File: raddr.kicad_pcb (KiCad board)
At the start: 2 copper layers, 25.4 x 25.4 mm, 7 parts, among them U1 PY32F002AL1xS

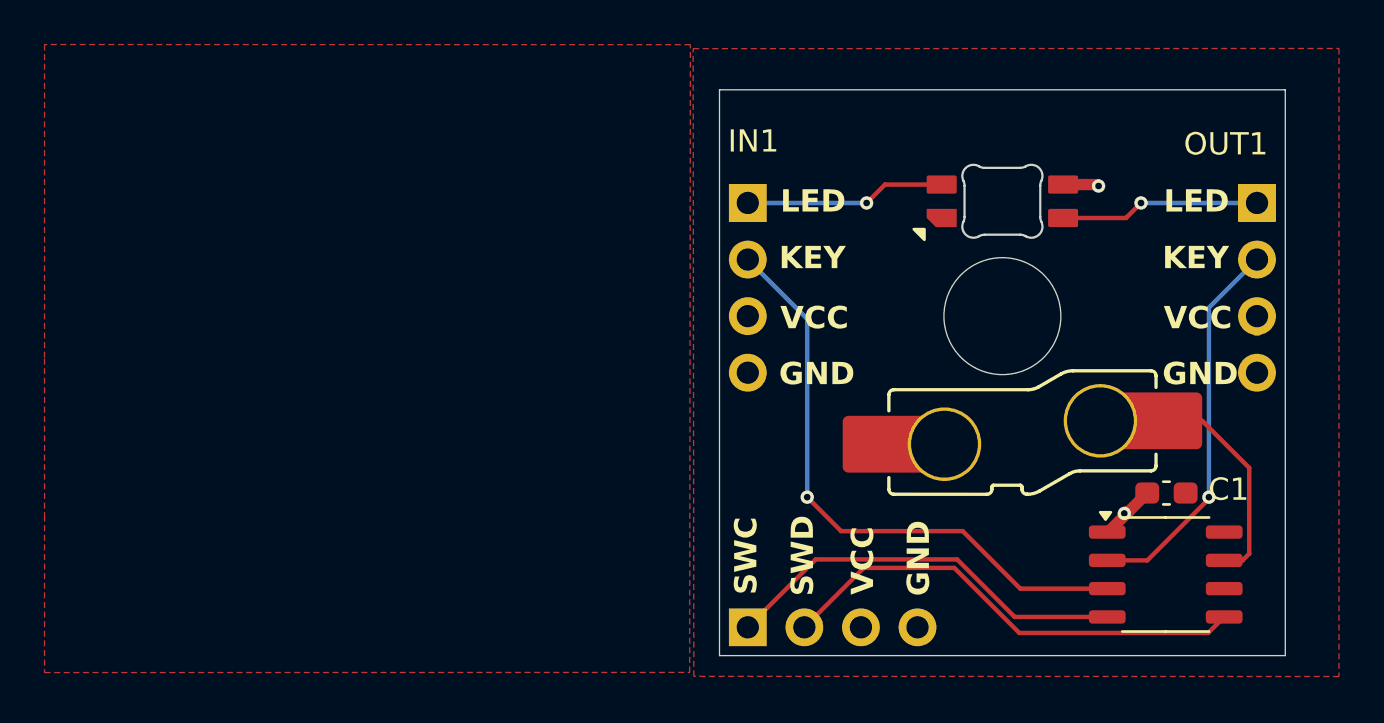
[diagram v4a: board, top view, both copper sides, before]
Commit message: fix power plane
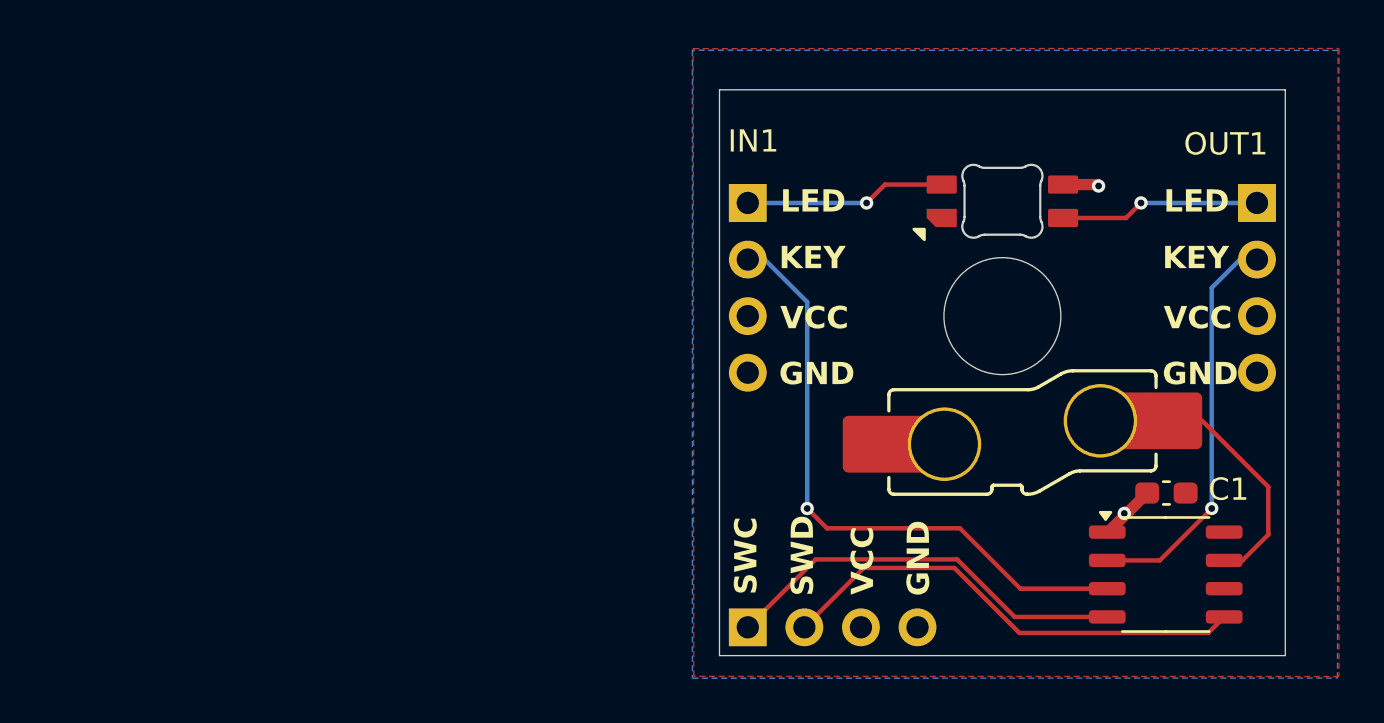
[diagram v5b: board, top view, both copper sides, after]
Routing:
- net KEY_DOUT: track 17.5 -> 18.3 mm
- net KEY_DIN: track 27.4 -> 28.2 mm
- net SWITCH: track 9.41 -> 10.1 mm
- net +5VD: track 4.93 -> 4.28 mm
- added copper zone on B.Cu, net +5VD
- removed copper zone on F.Cu, net +5VD
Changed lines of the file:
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@@
 		(tags "kailh choc 6028 rearmount rear mount led rgb backlight")
 		(property "Reference" "LED1"
-			(at 0 -2.6 360)
+			(at 0 -2.6 0)
 			(layer "F.SilkS")
 			(hide yes)
@@
 		)
 		(property "Value" "choc_SK6812MINI-E"
-			(at 0 18 360)
+			(at 0 18 0)
 			(layer "F.Fab")
 			(hide yes)
@@
 		(fp_arc
 			(start 1.699999 -0.702841)
-			(mid 1.71253 -0.814066)
+			(mid 1.712533 -0.814065)
 			(end 1.749484 -0.919719)
 			(stroke
@@
 		(tags "SOP SO")
 		(property "Reference" "U1"
-			(at 0 -3.4 360)
+			(at 0 -3.4 0)
 			(layer "F.SilkS")
 			(hide yes)
@@
 		)
 		(property "Value" "PY32F002AL1xS"
-			(at 0 3.4 360)
+			(at 0 3.4 0)
 			(layer "F.Fab")
 			(hide yes)
@@
 		)
 		(fp_text user "${REFERENCE}"
-			(at 0 0 360)
+			(at 0 0 0)
 			(layer "F.Fab")
 			(effects
@@
 		(fp_arc
 			(start 0.803483 7.591366)
-			(mid 0.856539 7.613325)
+			(mid 0.856533 7.613316)
 			(end 0.878483 7.666366)
 			(stroke
@@
 		(fp_arc
 			(start 2.63142 2.597493)
-			(mid 2.890651 2.490108)
+			(mid 2.890649 2.490103)
 			(end 3.168841 2.453491)
 			(stroke
@@
 		(fp_arc
 			(start 3.023183 7.070426)
-			(mid 3.246257 6.978023)
+			(mid 3.246259 6.978033)
 			(end 3.485647 6.946509)
 			(stroke
@@
 		(fp_arc
 			(start 0.803483 7.591366)
-			(mid 0.856539 7.613325)
+			(mid 0.856533 7.613316)
 			(end 0.878483 7.666366)
 			(stroke
@@
 		(fp_arc
 			(start 2.63142 2.597493)
-			(mid 2.890651 2.490108)
+			(mid 2.890649 2.490103)
 			(end 3.168841 2.453491)
 			(stroke
@@
 		(fp_arc
 			(start 3.023183 7.070426)
-			(mid 3.246257 6.978023)
+			(mid 3.246259 6.978033)
 			(end 3.485647 6.946509)
 			(stroke
@@
 		(fp_arc
 			(start 0.803483 7.591366)
-			(mid 0.856539 7.613325)
+			(mid 0.856533 7.613316)
 			(end 0.878483 7.666366)
 			(stroke
@@
 		(fp_arc
 			(start 2.63142 2.597493)
-			(mid 2.890651 2.490108)
+			(mid 2.890649 2.490103)
 			(end 3.168841 2.453491)
 			(stroke
@@
 		(fp_arc
 			(start 3.023183 7.070426)
-			(mid 3.246257 6.978023)
+			(mid 3.246259 6.978033)
 			(end 3.485647 6.946509)
 			(stroke
@@
 		)
 		(property "Value" "C_Polarized"
-			(at 0 1.43 360)
+			(at 0 1.43 0)
 			(layer "F.Fab")
 			(hide yes)
@@
 		)
 		(fp_text user "${REFERENCE}"
-			(at 0 0 360)
+			(at 0 0 0)
 			(layer "F.Fab")
 			(effects
@@
 	)
 	(segment
-		(start 20.32 5.08)
-		(end 20.32 5.725506)
-		(width 0.508)
-		(layer "B.Cu")
-		(net 2)
-	)
-	(segment
 		(start 19.6462 0.6738)
 		(end 20.32 0)
@@
 	(segment
 		(start 13.5968 16.0448)
-		(end 15.396522 16.0448)
-		(width 0.2)
-		(layer "F.Cu")
-		(net 4)
-	)
-	(segment
-		(start 18.161 13.280322)
-		(end 18.161 13.208)
+		(end 15.9592 16.0448)
 		(width 0.2)
 		(layer "F.Cu")
@@
 	)
 	(segment
-		(start 15.396522 16.0448)
-		(end 18.161 13.280322)
+		(start 15.9592 16.0448)
+		(end 18.288 13.716)
 		(width 0.2)
 		(layer "F.Cu")
@@
 	)
 	(via
-		(at 18.161 13.208)
+		(at 18.288 13.716)
 		(size 0.6)
 		(drill 0.3)
@@
 	)
 	(segment
-		(start 18.161 4.699)
-		(end 18.161 13.208)
+		(start 18.288 3.81)
+		(end 18.288 13.716)
 		(width 0.2)
 		(layer "B.Cu")
@@
 	(segment
 		(start 20.32 2.54)
-		(end 18.161 4.699)
+		(end 19.558 2.54)
+		(width 0.2)
+		(layer "B.Cu")
+		(net 4)
+	)
+	(segment
+		(start 19.558 2.54)
+		(end 18.288 3.81)
 		(width 0.2)
 		(layer "B.Cu")
@@
 	(segment
 		(start 9.6948 17.3148)
-		(end 7.112 14.732)
-		(width 0.2)
-		(layer "F.Cu")
-		(net 6)
-	)
-	(segment
-		(start 13.5968 17.3148)
-		(end 9.6948 17.3148)
+		(end 6.985 14.605)
 		(width 0.2)
 		(layer "F.Cu")
@@
 	)
 	(segment
-		(start 1.651 14.732)
-		(end 0.127 13.208)
+		(start 6.985 14.605)
+		(end 1.016004 14.605)
 		(width 0.2)
 		(layer "F.Cu")
@@
 	)
 	(segment
-		(start 7.112 14.732)
-		(end 1.651 14.732)
+		(start 13.5968 17.3148)
+		(end 9.6948 17.3148)
 		(width 0.2)
 		(layer "F.Cu")
@@
 		(net 6)
 	)
+	(segment
+		(start 1.016004 14.605)
+		(end 0.127 13.715996)
+		(width 0.2)
+		(layer "F.Cu")
+		(net 6)
+	)
 	(via
-		(at 0.127 13.208)
+		(at 0.127 13.715996)
 		(size 0.6)
 		(drill 0.3)
@@
 	)
 	(segment
-		(start 0.127 5.207)
-		(end 0.127 13.208)
+		(start -2.54 2.54)
+		(end -1.778 2.54)
 		(width 0.2)
 		(layer "B.Cu")
@@
 	)
 	(segment
-		(start -2.54 2.54)
-		(end 0.127 5.207)
+		(start 0.127 4.445)
+		(end 0.127 13.715996)
 		(width 0.2)
 		(layer "B.Cu")
@@
 	)
 	(segment
-		(start 19.9718 11.891801)
-		(end 19.9718 15.744799)
+		(start -1.778 2.54)
+		(end 0.127 4.445)
+		(width 0.2)
+		(layer "B.Cu")
+		(net 6)
+	)
+	(segment
+		(start 16.535 9.78)
+		(end 17.859999 9.78)
 		(width 0.2)
 		(layer "F.Cu")
@@
 	(segment
 		(start 17.859999 9.78)
-		(end 19.9718 11.891801)
+		(end 20.828 12.748001)
 		(width 0.2)
 		(layer "F.Cu")
@@
 	)
 	(segment
-		(start 19.9718 15.744799)
+		(start 20.828 14.888599)
 		(end 19.671799 16.0448)
 		(width 0.2)
@@
 	)
 	(segment
-		(start 16.535 9.78)
-		(end 17.859999 9.78)
+		(start 20.828 12.748001)
+		(end 20.828 14.888599)
 		(width 0.2)
 		(layer "F.Cu")
@@
 	)
 	(zone
-		(net 2)
-		(net_name "+5VD")
+		(net 1)
+		(net_name "GND")
 		(layer "F.Cu")
-		(name "POWER plane")
+		(name "Ground plane")
 		(hatch edge 0.5)
 		(connect_pads
@@
 		(polygon
 			(pts
-				(xy -5.117238 -7.105483) (xy -34.110476 -7.112) (xy -34.110476 6.985) (xy -34.110476 14.0335) (xy -34.110476 21.082)
-				(xy -5.148316 21.075184)
+				(xy -4.993238 -6.928883) (xy 24 -6.9354) (xy 24 21.2586) (xy -4.96216 21.251784)
 			)
 		)
 	)
 	(zone
-		(net 1)
-		(net_name "GND")
-		(layer "F.Cu")
-		(name "Ground plane")
+		(net 2)
+		(net_name "+5VD")
+		(layer "B.Cu")
+		(name "POWER plane")
 		(hatch edge 0.5)
 		(connect_pads
@@
 		(polygon
 			(pts
-				(xy -4.993238 -6.928883) (xy 24 -6.9354) (xy 24 21.2586) (xy -4.96216 21.251784)
+				(xy 23.965762 -6.851483) (xy -5.027476 -6.858) (xy -5.027476 7.239) (xy -5.027476 14.2875) (xy -5.027476 21.336)
+				(xy 23.934684 21.329184)
 			)
 		)

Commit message: silk screen and stuff
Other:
- board text added: "RABIES rev 1/N WFP-YBS 20241030 {dblquote}Waarschijnlijk ruk{dblquote}"
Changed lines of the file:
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@@
 			(plot_on_all_layers_selection 0x0000000_00000000)
 			(disableapertmacros no)
-			(usegerberextensions no)
-			(usegerberattributes yes)
-			(usegerberadvancedattributes yes)
-			(creategerberjobfile yes)
+			(usegerberextensions yes)
+			(usegerberattributes no)
+			(usegerberadvancedattributes no)
+			(creategerberjobfile no)
 			(dashed_line_dash_ratio 12.000000)
 			(dashed_line_gap_ratio 3.000000)
@@
 			(psa4output no)
 			(plotreference yes)
-			(plotvalue yes)
+			(plotvalue no)
 			(plotfptext yes)
 			(plotinvisibletext no)
 			(sketchpadsonfab no)
-			(subtractmaskfromsilk no)
+			(subtractmaskfromsilk yes)
 			(outputformat 1)
 			(mirror no)
-			(drillshape 1)
+			(drillshape 0)
 			(scaleselection 1)
 			(outputdirectory "")
@@
 		(fp_arc
 			(start 1.699999 -0.702841)
-			(mid 1.712533 -0.814065)
+			(mid 1.712531 -0.814066)
 			(end 1.749484 -0.919719)
 			(stroke
@@
 		(fp_arc
 			(start 2.63142 2.597493)
-			(mid 2.890649 2.490103)
+			(mid 2.890648 2.490104)
 			(end 3.168841 2.453491)
 			(stroke
@@
 		(fp_arc
 			(start 3.023183 7.070426)
-			(mid 3.246259 6.978033)
+			(mid 3.246261 6.978038)
 			(end 3.485647 6.946509)
 			(stroke
@@
 		(fp_arc
 			(start 2.63142 2.597493)
-			(mid 2.890649 2.490103)
+			(mid 2.890648 2.490104)
 			(end 3.168841 2.453491)
 			(stroke
@@
 		(fp_arc
 			(start 3.023183 7.070426)
-			(mid 3.246259 6.978033)
+			(mid 3.246261 6.978038)
 			(end 3.485647 6.946509)
 			(stroke
@@
 		(fp_arc
 			(start 2.63142 2.597493)
-			(mid 2.890649 2.490103)
+			(mid 2.890648 2.490104)
 			(end 3.168841 2.453491)
 			(stroke
@@
 		(fp_arc
 			(start 3.023183 7.070426)
-			(mid 3.246259 6.978033)
+			(mid 3.246261 6.978038)
 			(end 3.485647 6.946509)
 			(stroke
@@
 		(layer "Edge.Cuts")
 	)
+	(gr_text "RABIES rev 1/N\nWFP-YBS\n20241030\n{dblquote}Waarschijnlijk ruk{dblquote}\n"
+		(at 13.843 19.685 0)
+		(layer "B.SilkS")
+		(effects
+			(font
+				(size 1 1)
+				(thickness 0.2)
+				(bold yes)
+			)
+			(justify bottom mirror)
+		)
+	)
 	(gr_text "SWD"
